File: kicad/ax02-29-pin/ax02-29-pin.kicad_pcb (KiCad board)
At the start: 4 copper layers, 20 x 20 mm, 4 parts, among them CN1 Leafony Bus, J2 Conn_02x05_Top_Bottom, J3 Conn_02x05_Top_Bottom, J4 Conn_02x05_Top_Bottom

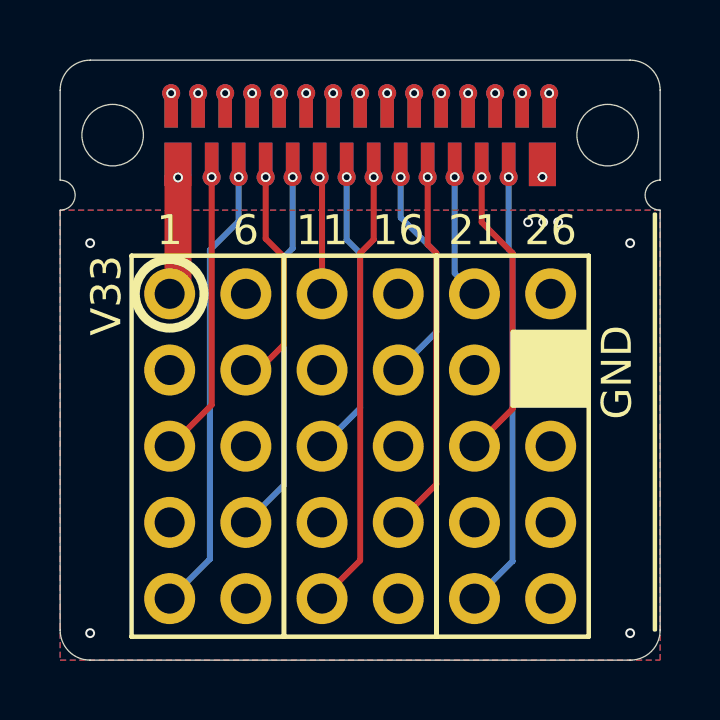
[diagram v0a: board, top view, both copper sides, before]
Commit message: 面付方法を変更
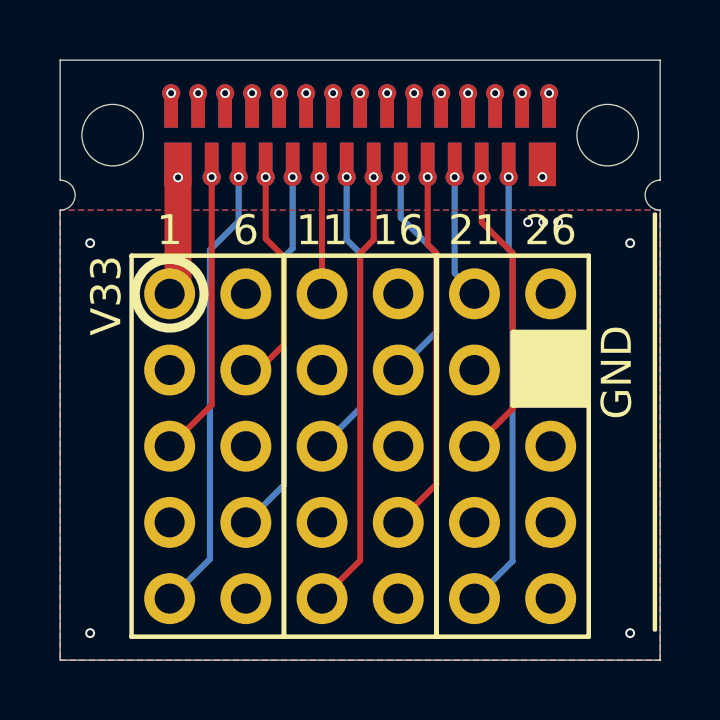
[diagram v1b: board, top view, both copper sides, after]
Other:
- outline, holes or cut-outs redrawn
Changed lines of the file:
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@@
 	)
 	(gr_line
-		(start 25 26)
+		(start 25 25)
 		(end 25 29)
 		(stroke
@@
 		(layer "Edge.Cuts")
 	)
-	(gr_arc
-		(start 25 26)
-		(mid 25.292893 25.292893)
-		(end 26 25)
+	(gr_line
+		(start 25 25)
+		(end 45 25)
 		(stroke
 			(width 0.01)
@@
 	(gr_line
 		(start 25 30)
-		(end 25 44)
+		(end 25 45)
 		(stroke
 			(width 0.01)
@@
 	)
 	(gr_line
-		(start 26 25)
-		(end 44 25)
-		(stroke
-			(width 0.01)
-			(type solid)
-		)
-		(layer "Edge.Cuts")
-	)
-	(gr_arc
-		(start 26 45)
-		(mid 25.292893 44.707107)
-		(end 25 44)
-		(stroke
-			(width 0.01)
-			(type solid)
-		)
-		(layer "Edge.Cuts")
-	)
-	(gr_arc
-		(start 44 25)
-		(mid 44.707107 25.292893)
-		(end 45 26)
-		(stroke
-			(width 0.01)
-			(type solid)
-		)
-		(layer "Edge.Cuts")
-	)
-	(gr_line
-		(start 44 45)
-		(end 26 45)
-		(stroke
-			(width 0.01)
-			(type default)
-		)
-		(layer "Edge.Cuts")
-	)
-	(gr_line
-		(start 45 26)
+		(start 45 25)
 		(end 45 29)
 		(stroke
@@
 	(gr_line
 		(start 45 30)
-		(end 45 44)
+		(end 45 45)
 		(stroke
 			(width 0.01)
@@
 		(layer "Edge.Cuts")
 	)
-	(gr_arc
-		(start 45 44)
-		(mid 44.707107 44.707107)
-		(end 44 45)
+	(gr_line
+		(start 45 45)
+		(end 25 45)
 		(stroke
 			(width 0.01)
-			(type solid)
+			(type default)
 		)
 		(layer "Edge.Cuts")
@@
 	)
 	(zone
+		(net "/F19")
+		(layer "F.Cu")
+		(hatch none 0.1)
+		(priority 30003)
+		(attr
+			(teardrop
+				(type padvia)
+			)
+		)
+		(connect_pads yes
+			(clearance 0)
+		)
+		(min_thickness 0.0254)
+		(fill yes
+			(island_removal_mode 1)
+		)
+		(polygon
+			(pts
+				(xy 37.15 29.422433) (xy 37.35 29.422433) (xy 37.475 29.095634) (xy 37.25 28.324) (xy 37.025 29.095634)
+			)
+		)
+	)
+	(zone
+		(net "/F23")
+		(layer "F.Cu")
+		(hatch none 0.1)
+		(priority 30001)
+		(attr
+			(teardrop
+				(type padvia)
+			)
+		)
+		(connect_pads yes
+			(clearance 0)
+		)
+		(min_thickness 0.0254)
+		(fill yes
+			(island_removal_mode 1)
+		)
+		(polygon
+			(pts
+				(xy 38.95 29.422433) (xy 39.15 29.422433) (xy 39.275 29.095634) (xy 39.05 28.324) (xy 38.825 29.095634)
+			)
+		)
+	)
+	(zone
+		(net "/F11")
+		(layer "F.Cu")
+		(hatch none 0.1)
+		(priority 30005)
+		(attr
+			(teardrop
+				(type padvia)
+			)
+		)
+		(connect_pads yes
+			(clearance 0)
+		)
+		(min_thickness 0.0254)
+		(fill yes
+			(island_removal_mode 1)
+		)
+		(polygon
+			(pts
+				(xy 33.63 29.41149) (xy 33.83 29.41149) (xy 33.947433 28.939158) (xy 33.73 28.324) (xy 33.505 29.15973)
+			)
+		)
+	)
+	(zone
+		(net "/F3")
+		(layer "F.Cu")
+		(hatch none 0.1)
+		(priority 30000)
+		(attr
+			(teardrop
+				(type padvia)
+			)
+		)
+		(connect_pads yes
+			(clearance 0)
+		)
+		(min_thickness 0.0254)
+		(fill yes
+			(island_removal_mode 1)
+		)
+		(polygon
+			(pts
+				(xy 29.95 29.422433) (xy 30.15 29.422433) (xy 30.275 29.095634) (xy 30.05 28.324) (xy 29.825 29.095634)
+			)
+		)
+	)
+	(zone
 		(net "/F7")
 		(layer "F.Cu")
@@
 			(pts
 				(xy 35.35 29.422433) (xy 35.55 29.422433) (xy 35.675 29.095634) (xy 35.45 28.324) (xy 35.225 29.095634)
-			)
-		)
-	)
-	(zone
-		(net "/F19")
-		(layer "F.Cu")
-		(hatch none 0.1)
-		(priority 30003)
-		(attr
-			(teardrop
-				(type padvia)
-			)
-		)
-		(connect_pads yes
-			(clearance 0)
-		)
-		(min_thickness 0.0254)
-		(fill yes
-			(island_removal_mode 1)
-		)
-		(polygon
-			(pts
-				(xy 37.15 29.422433) (xy 37.35 29.422433) (xy 37.475 29.095634) (xy 37.25 28.324) (xy 37.025 29.095634)
-			)
-		)
-	)
-	(zone
-		(net "/F23")
-		(layer "F.Cu")
-		(hatch none 0.1)
-		(priority 30001)
-		(attr
-			(teardrop
-				(type padvia)
-			)
-		)
-		(connect_pads yes
-			(clearance 0)
-		)
-		(min_thickness 0.0254)
-		(fill yes
-			(island_removal_mode 1)
-		)
-		(polygon
-			(pts
-				(xy 38.95 29.422433) (xy 39.15 29.422433) (xy 39.275 29.095634) (xy 39.05 28.324) (xy 38.825 29.095634)
-			)
-		)
-	)
-	(zone
-		(net "/F11")
-		(layer "F.Cu")
-		(hatch none 0.1)
-		(priority 30005)
-		(attr
-			(teardrop
-				(type padvia)
-			)
-		)
-		(connect_pads yes
-			(clearance 0)
-		)
-		(min_thickness 0.0254)
-		(fill yes
-			(island_removal_mode 1)
-		)
-		(polygon
-			(pts
-				(xy 33.63 29.41149) (xy 33.83 29.41149) (xy 33.947433 28.939158) (xy 33.73 28.324) (xy 33.505 29.15973)
-			)
-		)
-	)
-	(zone
-		(net "/F3")
-		(layer "F.Cu")
-		(hatch none 0.1)
-		(priority 30000)
-		(attr
-			(teardrop
-				(type padvia)
-			)
-		)
-		(connect_pads yes
-			(clearance 0)
-		)
-		(min_thickness 0.0254)
-		(fill yes
-			(island_removal_mode 1)
-		)
-		(polygon
-			(pts
-				(xy 29.95 29.422433) (xy 30.15 29.422433) (xy 30.275 29.095634) (xy 30.05 28.324) (xy 29.825 29.095634)
 			)
 		)
@@
 	)
 	(zone
+		(net "/F9")
+		(layer "B.Cu")
+		(hatch none 0.1)
+		(priority 30005)
+		(attr
+			(teardrop
+				(type padvia)
+			)
+		)
+		(connect_pads yes
+			(clearance 0)
+		)
+		(min_thickness 0.0254)
+		(fill yes
+			(island_removal_mode 1)
+		)
+		(polygon
+			(pts
+				(xy 32.65 29.422433) (xy 32.85 29.422433) (xy 32.975 29.095634) (xy 32.75 28.324) (xy 32.525 29.095634)
+			)
+		)
+	)
+	(zone
+		(net "/F21")
+		(layer "B.Cu")
+		(hatch none 0.1)
+		(priority 30001)
+		(attr
+			(teardrop
+				(type padvia)
+			)
+		)
+		(connect_pads yes
+			(clearance 0)
+		)
+		(min_thickness 0.0254)
+		(fill yes
+			(island_removal_mode 1)
+		)
+		(polygon
+			(pts
+				(xy 38.05 29.422433) (xy 38.25 29.422433) (xy 38.375 29.095634) (xy 38.15 28.324) (xy 37.925 29.095634)
+			)
+		)
+	)
+	(zone
 		(net "/F25")
 		(layer "B.Cu")
@@
 	)
 	(zone
+		(net "/F13")
+		(layer "B.Cu")
+		(hatch none 0.1)
+		(priority 30002)
+		(attr
+			(teardrop
+				(type padvia)
+			)
+		)
+		(connect_pads yes
+			(clearance 0)
+		)
+		(min_thickness 0.0254)
+		(fill yes
+			(island_removal_mode 1)
+		)
+		(polygon
+			(pts
+				(xy 34.45 29.422433) (xy 34.65 29.422433) (xy 34.775 29.095634) (xy 34.55 28.324) (xy 34.325 29.095634)
+			)
+		)
+	)
+	(zone
 		(net "/F5")
 		(layer "B.Cu")
@@
 			)
 		)
-	)
-	(zone
-		(net "/F13")
-		(layer "B.Cu")
-		(hatch none 0.1)
-		(priority 30002)
-		(attr
-			(teardrop
-				(type padvia)
-			)
-		)
-		(connect_pads yes
-			(clearance 0)
-		)
-		(min_thickness 0.0254)
-		(fill yes
-			(island_removal_mode 1)
-		)
-		(polygon
-			(pts
-				(xy 34.45 29.422433) (xy 34.65 29.422433) (xy 34.775 29.095634) (xy 34.55 28.324) (xy 34.325 29.095634)
-			)
-		)
-	)
-	(zone
-		(net "/F21")
-		(layer "B.Cu")
-		(hatch none 0.1)
-		(priority 30001)
-		(attr
-			(teardrop
-				(type padvia)
-			)
-		)
-		(connect_pads yes
-			(clearance 0)
-		)
-		(min_thickness 0.0254)
-		(fill yes
-			(island_removal_mode 1)
-		)
-		(polygon
-			(pts
-				(xy 38.05 29.422433) (xy 38.25 29.422433) (xy 38.375 29.095634) (xy 38.15 28.324) (xy 37.925 29.095634)
-			)
-		)
-	)
-	(zone
-		(net "/F9")
-		(layer "B.Cu")
-		(hatch none 0.1)
-		(priority 30005)
-		(attr
-			(teardrop
-				(type padvia)
-			)
-		)
-		(connect_pads yes
-			(clearance 0)
-		)
-		(min_thickness 0.0254)
-		(fill yes
-			(island_removal_mode 1)
-		)
-		(polygon
-			(pts
-				(xy 32.65 29.422433) (xy 32.85 29.422433) (xy 32.975 29.095634) (xy 32.75 28.324) (xy 32.525 29.095634)
-			)
-		)
